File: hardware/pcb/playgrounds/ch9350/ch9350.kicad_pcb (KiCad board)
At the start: 2 copper layers, 50.8 x 76.2 mm, 35 parts, among them J1 TYPE-C-31-M-12, J2 USB-U267-BWS, J3 Conn_02x08_Odd_Even, J4 Conn_02x10_Odd_Even, J5 Conn_02x10_Odd_Even, Q1 MMBT2222A, Q2 MMBT2222A, Q3 MMBT2222A, Q4 MMBT2222A, Q5 MMBT2222A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

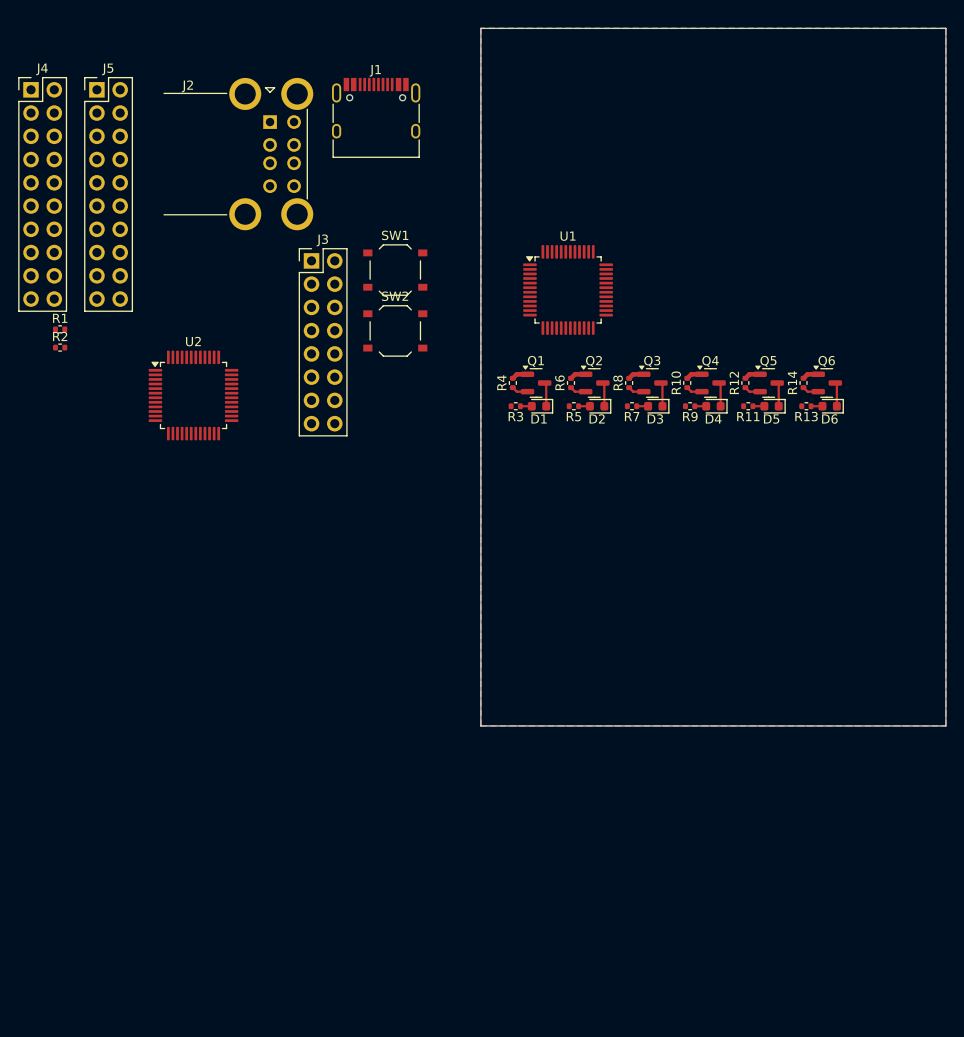
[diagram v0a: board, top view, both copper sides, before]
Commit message: ch9350 devboard layout
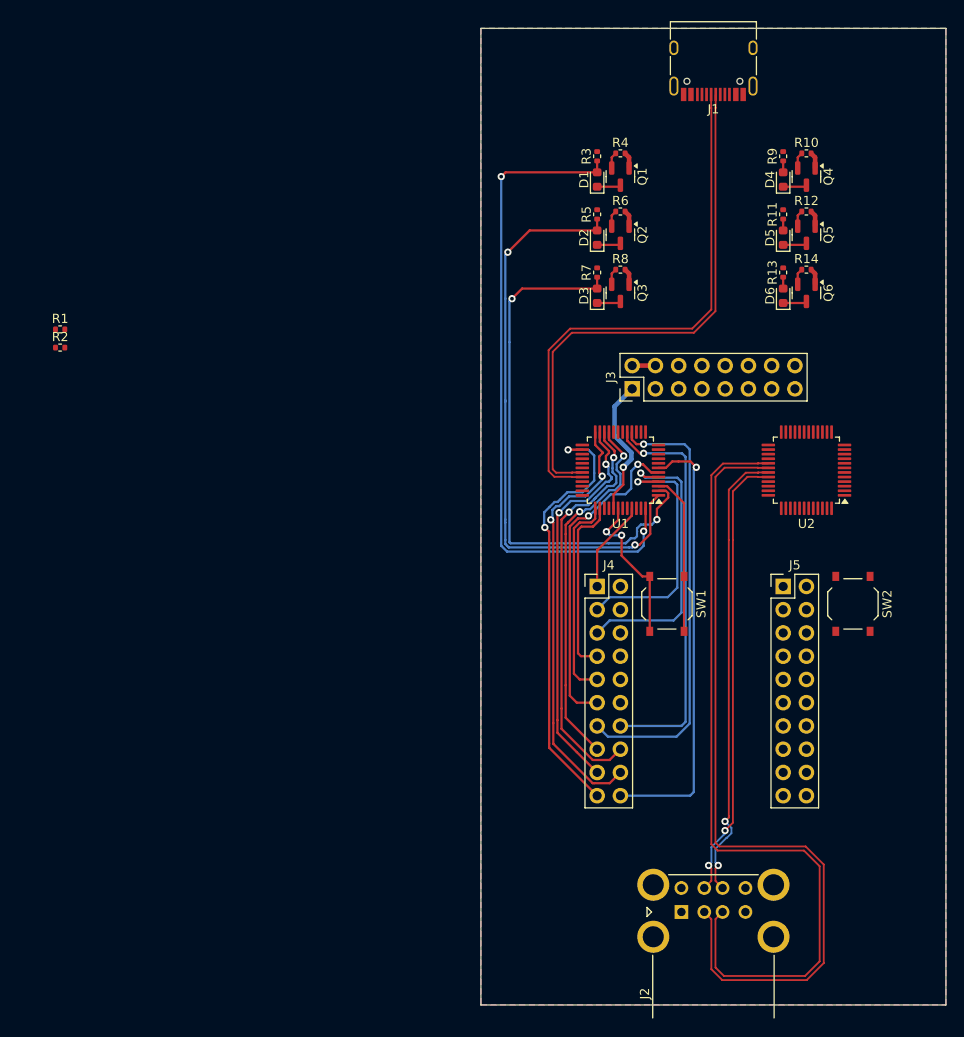
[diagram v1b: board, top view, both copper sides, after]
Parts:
- moved J2 97.3 mm to (148.9, 147.3), turned to 90 degrees
- moved J5 92.5 mm to (160.0, 111.8)
- moved J4 82.3 mm to (139.7, 111.8)
- moved U2 67.4 mm to (162.6, 99.1), turned to 180 degrees
- moved SW2 58.2 mm to (167.6, 113.7), turned to -90 degrees
- moved SW1 47.0 mm to (147.3, 113.7), turned to -90 degrees
- moved J3 37.7 mm to (143.5, 90.2), turned to 90 degrees
- moved J1 37.5 mm to (152.4, 54.0), turned to 180 degrees
- moved R9 29.1 mm to (160.0, 64.8), turned to 90 degrees
- moved R3 28.7 mm to (139.7, 64.8), turned to 90 degrees
- moved R10 28.3 mm to (162.6, 64.5), turned to 0 degrees
- moved R4 27.7 mm to (142.2, 64.5), turned to 0 degrees
- moved D4 25.9 mm to (160.0, 67.3), turned to 90 degrees
- moved D1 25.6 mm to (139.7, 67.3), turned to 90 degrees
- moved Q4 24.9 mm to (162.6, 67.0), turned to -90 degrees
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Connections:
- net /DM renamed /D-
- net /DM1 renamed /D1-
- net /DM2 renamed /D2-
- net /DP renamed /D+
- net /DP1 renamed /D1+
- net /DP2 renamed /D2+
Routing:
- net /D1-: track 0.00 -> 89.8 mm
- net /D1+: track 0.00 -> 89.1 mm
- net /LED0a: track 1.24 -> 72.5 mm, vias 0 -> 2
- net /LED1a: track 1.24 -> 65.2 mm, vias 0 -> 2
- net /D-: track 0.00 -> 60.3 mm
- net /D+: track 0.00 -> 59.5 mm
- net /LED2a: track 1.24 -> 60.0 mm, vias 0 -> 2
- net /D2+: track 0.00 -> 50.4 mm, vias 0 -> 2
- net /D2-: track 0.00 -> 49.4 mm, vias 0 -> 2
- net /XIa: track 0.00 -> 48.7 mm, vias 0 -> 1
- net /DEBUGa: track 0.00 -> 48.5 mm, vias 0 -> 1
- net /IO4a: track 0.00 -> 48.0 mm, vias 0 -> 2
- net /TNOWa: track 0.00 -> 47.7 mm, vias 0 -> 2
- net /IO2a: track 0.00 -> 45.3 mm, vias 0 -> 2
- net /XOa: track 0.00 -> 44.3 mm, vias 0 -> 1
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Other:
- board size 50.8 x 76.2 mm -> 50.8 x 106.7 mm

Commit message: ch9350 devboard layout
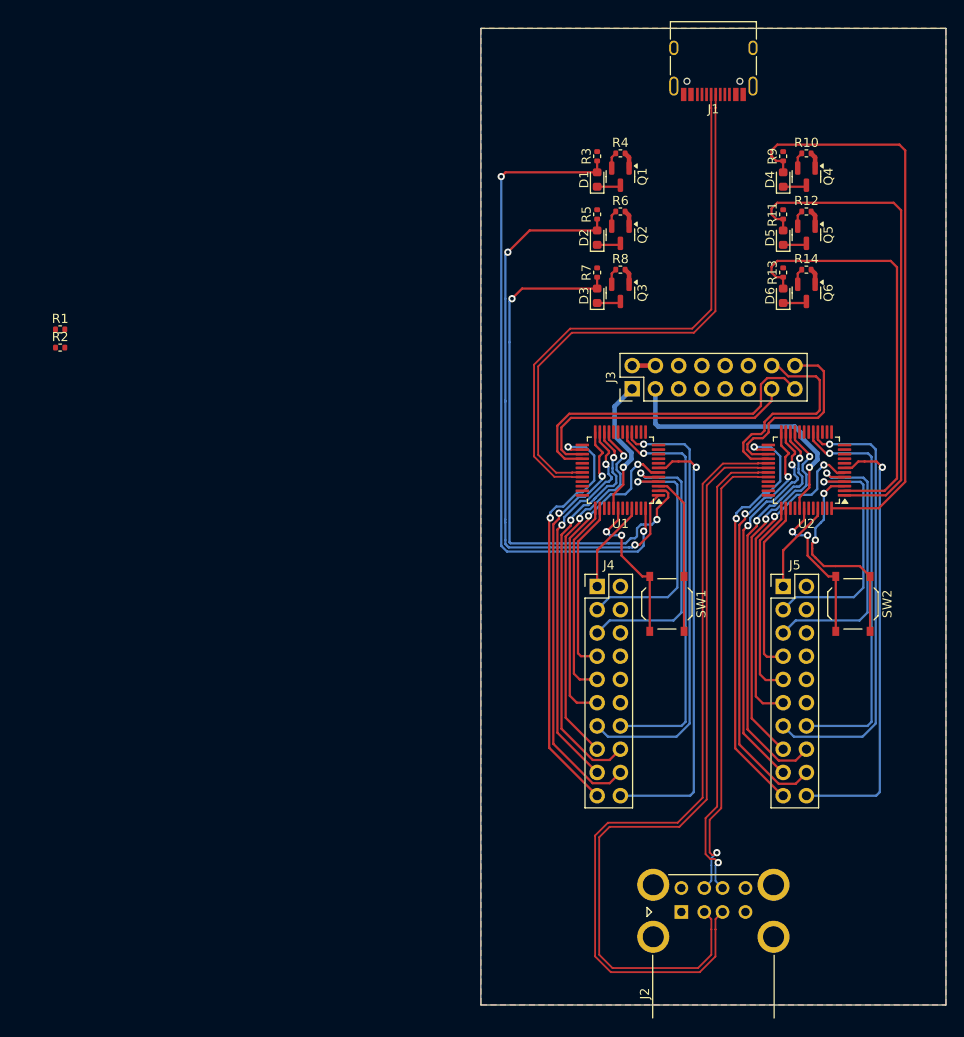
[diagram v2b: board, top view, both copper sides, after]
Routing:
- net /LED0b: track 1.24 -> 63.9 mm
- net /LED1b: track 1.24 -> 54.5 mm
- net /XIb: track 0.00 -> 48.7 mm, vias 0 -> 1
- net /DEBUGb: track 0.00 -> 48.5 mm, vias 0 -> 1
- net /IO4b: track 0.00 -> 47.1 mm, vias 0 -> 2
- net /TNOWb: track 0.00 -> 47.1 mm, vias 0 -> 2
- net /LED2b: track 1.24 -> 47.0 mm
- net /IO2b: track 0.00 -> 44.8 mm, vias 0 -> 2
- net /XOb: track 0.00 -> 44.3 mm, vias 0 -> 1
- net /IO3b: track 0.00 -> 42.8 mm, vias 0 -> 2
- net /IO1b: track 0.00 -> 40.3 mm, vias 0 -> 2
- net /TXDa: track 0.00 -> 35.8 mm
- net /xOSCb: track 0.00 -> 35.3 mm, vias 0 -> 2
- net /S1b: track 0.00 -> 31.4 mm, vias 0 -> 1
- net /RXDa: track 0.00 -> 30.4 mm
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
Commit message: ch9350 devboard layout
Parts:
- moved R1 77.3 mm to (154.7, 60.3)
- moved R2 73.3 mm to (149.9, 60.3), turned to 180 degrees
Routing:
- net /VBUS: track 2.54 -> 184.8 mm, vias 0 -> 2
- net GNDPWR: track 0.00 -> 25.5 mm
- net GND: track 10.7 -> 15.6 mm
- net /CC1: track 0.00 -> 2.55 mm
- net /CC2: track 0.00 -> 2.42 mm
- net /TXDb: track 23.6 -> 23.0 mm

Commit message: ch9350 devboard layout 2
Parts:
- removed D1, D2, D3, D4, D5, D6: 19-213/Y2C-CQ2R2L/3T(CY), LED_SMD:LED_0603_1608Metric
- removed J1: TYPE-C-31-M-12, Connector_USB:USB_C_Receptacle_HRO_TYPE-C-31-M-12
- removed J2: USB-U267-BWS, Connector_USB:USB_A_CUI_UJ2-ADH-TH_Horizontal_Stacked
- removed J3: Conn_02x08_Odd_Even, Connector_PinHeader_2.54mm:PinHeader_2x08_P2.54mm_Vertical
- removed J4, J5: Conn_02x10_Odd_Even, Connector_PinHeader_2.54mm:PinHeader_2x10_P2.54mm_Vertical
- removed Q1, Q2, Q3, Q4, Q5, Q6: MMBT2222A, Package_TO_SOT_SMD:SOT-23
- removed R1, R2: 5K1, Resistor_SMD:R_0402_1005Metric
- removed R10, R12, R14, R4, R6, R8: 6K2, Resistor_SMD:R_0402_1005Metric
- removed R11, R13, R3, R5, R7, R9: 1K, Resistor_SMD:R_0402_1005Metric
- removed SW1, SW2: TS-1187A-B-A-B, Button_Switch_SMD:SW_Push_1P1T_XKB_TS-1187A
- removed U1, U2: CH9350, Package_QFP:LQFP-48_7x7mm_P0.5mm
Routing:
- net /VBUS: track 184.8 -> 0.00 mm, vias 2 -> 0
- net /D1+: track 88.8 -> 0.00 mm
- net /D1-: track 86.6 -> 0.00 mm
- net /LED0a: track 72.5 -> 0.00 mm, vias 2 -> 0
- net /LED1a: track 65.2 -> 0.00 mm, vias 2 -> 0
- net /LED0b: track 63.9 -> 0.00 mm
- net /D-: track 61.6 -> 0.00 mm
- net /D+: track 60.8 -> 0.00 mm
- net /LED2a: track 60.0 -> 0.00 mm, vias 2 -> 0
- net /LED1b: track 54.5 -> 0.00 mm
- net /D2+: track 51.9 -> 0.00 mm, vias 1 -> 0
- net /D2-: track 51.4 -> 0.00 mm, vias 1 -> 0
- net /XIa: track 48.7 -> 0.00 mm, vias 1 -> 0
- net /XIb: track 48.7 -> 0.00 mm, vias 1 -> 0
- net /DEBUGb: track 48.5 -> 0.00 mm, vias 1 -> 0
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
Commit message: ch9350 devboard layout 2
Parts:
- added D1: 19-213/Y2C-CQ2R2L/3T(CY), LED_SMD:LED_0603_1608Metric, F.Cu at (78.8, 79.5)
- added D2: 19-213/Y2C-CQ2R2L/3T(CY), LED_SMD:LED_0603_1608Metric, F.Cu at (78.8, 82.1)
- added D3: 19-213/Y2C-CQ2R2L/3T(CY), LED_SMD:LED_0603_1608Metric, F.Cu at (78.8, 84.7)
- added D4: 19-213/Y2C-CQ2R2L/3T(CY), LED_SMD:LED_0603_1608Metric, F.Cu at (78.8, 87.3)
- added D5: 19-213/Y2C-CQ2R2L/3T(CY), LED_SMD:LED_0603_1608Metric, F.Cu at (78.8, 89.9)
- added D6: 19-213/Y2C-CQ2R2L/3T(CY), LED_SMD:LED_0603_1608Metric, F.Cu at (78.8, 92.5)
- added J1: TYPE-C-31-M-12, Connector_USB:USB_C_Receptacle_HRO_TYPE-C-31-M-12, F.Cu at (152.4, 54.6)
- added J2: USB-U267-BWS, Connector_USB:USB_A_CUI_UJ2-ADH-TH_Horizontal_Stacked, F.Cu at (105.2, 56.6)
- added J3: Conn_02x08_Odd_Even, Connector_PinHeader_2.54mm:PinHeader_2x08_P2.54mm_Vertical, F.Cu at (143.5, 99.1)
- added J4: Conn_02x10_Odd_Even, Connector_PinHeader_2.54mm:PinHeader_2x10_P2.54mm_Vertical, F.Cu at (170.2, 67.3)
- added J5: Conn_02x10_Odd_Even, Connector_PinHeader_2.54mm:PinHeader_2x10_P2.54mm_Vertical, F.Cu at (86.3, 53.1)
- added Q1: MMBT2222A, Package_TO_SOT_SMD:SOT-23, F.Cu at (105.0, 71.8)
- added Q2: MMBT2222A, Package_TO_SOT_SMD:SOT-23, F.Cu at (105.0, 76.5)
- added Q3: MMBT2222A, Package_TO_SOT_SMD:SOT-23, F.Cu at (105.0, 81.1)
- added Q4: MMBT2222A, Package_TO_SOT_SMD:SOT-23, F.Cu at (105.0, 85.7)
- added Q5: MMBT2222A, Package_TO_SOT_SMD:SOT-23, F.Cu at (105.0, 90.3)
- added Q6: MMBT2222A, Package_TO_SOT_SMD:SOT-23, F.Cu at (105.0, 95.0)
- added R1: 5K1, Resistor_SMD:R_0402_1005Metric, F.Cu at (82.3, 79.2)
- added R10: 6K2, Resistor_SMD:R_0402_1005Metric, F.Cu at (85.2, 87.2)
- added R11: 1K, Resistor_SMD:R_0402_1005Metric, F.Cu at (88.1, 79.2)
- added R12: 6K2, Resistor_SMD:R_0402_1005Metric, F.Cu at (88.1, 81.2)
- added R13: 1K, Resistor_SMD:R_0402_1005Metric, F.Cu at (88.1, 83.2)
- added R14: 6K2, Resistor_SMD:R_0402_1005Metric, F.Cu at (88.1, 85.2)
- added R2: 5K1, Resistor_SMD:R_0402_1005Metric, F.Cu at (82.3, 81.2)
- added R3: 1K, Resistor_SMD:R_0402_1005Metric, F.Cu at (82.3, 83.2)
- added R4: 6K2, Resistor_SMD:R_0402_1005Metric, F.Cu at (82.3, 85.2)
- added R5: 1K, Resistor_SMD:R_0402_1005Metric, F.Cu at (82.3, 87.2)
- added R6: 6K2, Resistor_SMD:R_0402_1005Metric, F.Cu at (85.2, 79.2)
- added R7: 1K, Resistor_SMD:R_0402_1005Metric, F.Cu at (85.2, 81.2)
- added R8: 6K2, Resistor_SMD:R_0402_1005Metric, F.Cu at (85.2, 83.2)
- added R9: 1K, Resistor_SMD:R_0402_1005Metric, F.Cu at (85.2, 85.2)
- added SW1: TS-1187A-B-A-B, Button_Switch_SMD:SW_Push_1P1T_XKB_TS-1187A, F.Cu at (118.9, 72.8)
- added SW2: TS-1187A-B-A-B, Button_Switch_SMD:SW_Push_1P1T_XKB_TS-1187A, F.Cu at (118.9, 79.4)
- added U1: CH9350, Package_QFP:LQFP-48_7x7mm_P0.5mm, F.Cu at (152.4, 78.7)
- added U2: CH9350, Package_QFP:LQFP-48_7x7mm_P0.5mm, F.Cu at (96.9, 86.5)
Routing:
- net /VBUS: track 0.00 -> 53.8 mm, vias 0 -> 2
- net /VBUSa: track 0.00 -> 32.3 mm, vias 0 -> 3
- net /SELa: track 0.00 -> 31.5 mm, vias 0 -> 1
- net /DEBUGa: track 0.00 -> 31.2 mm, vias 0 -> 2
- net /RXDa: track 0.00 -> 29.6 mm, vias 0 -> 1
- net /TXDa: track 0.00 -> 28.0 mm, vias 0 -> 1
- net /S0a: track 0.00 -> 27.1 mm, vias 0 -> 2
- net /S1a: track 0.00 -> 25.9 mm, vias 0 -> 2
- net /TNOWa: track 0.00 -> 24.6 mm, vias 0 -> 1
- net /xOSCa: track 0.00 -> 24.4 mm, vias 0 -> 2
- net /BAUD0a: track 0.00 -> 23.4 mm, vias 0 -> 1
- net /BAUD1a: track 0.00 -> 23.2 mm, vias 0 -> 1
- net /XOa: track 0.00 -> 21.3 mm, vias 0 -> 2
- net /XIa: track 0.00 -> 18.6 mm, vias 0 -> 2
- net /D+: track 0.00 -> 18.6 mm
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
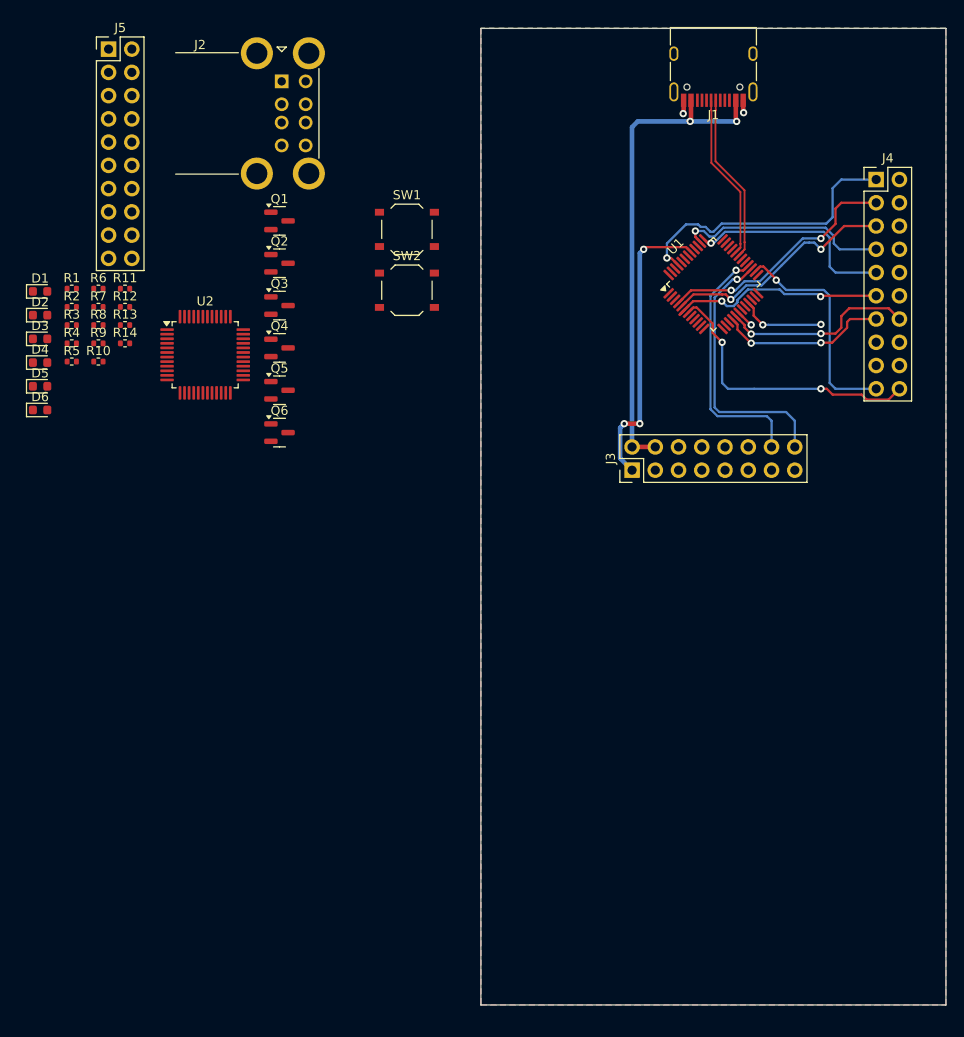
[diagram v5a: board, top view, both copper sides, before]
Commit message: ch9350 devboard layout 3
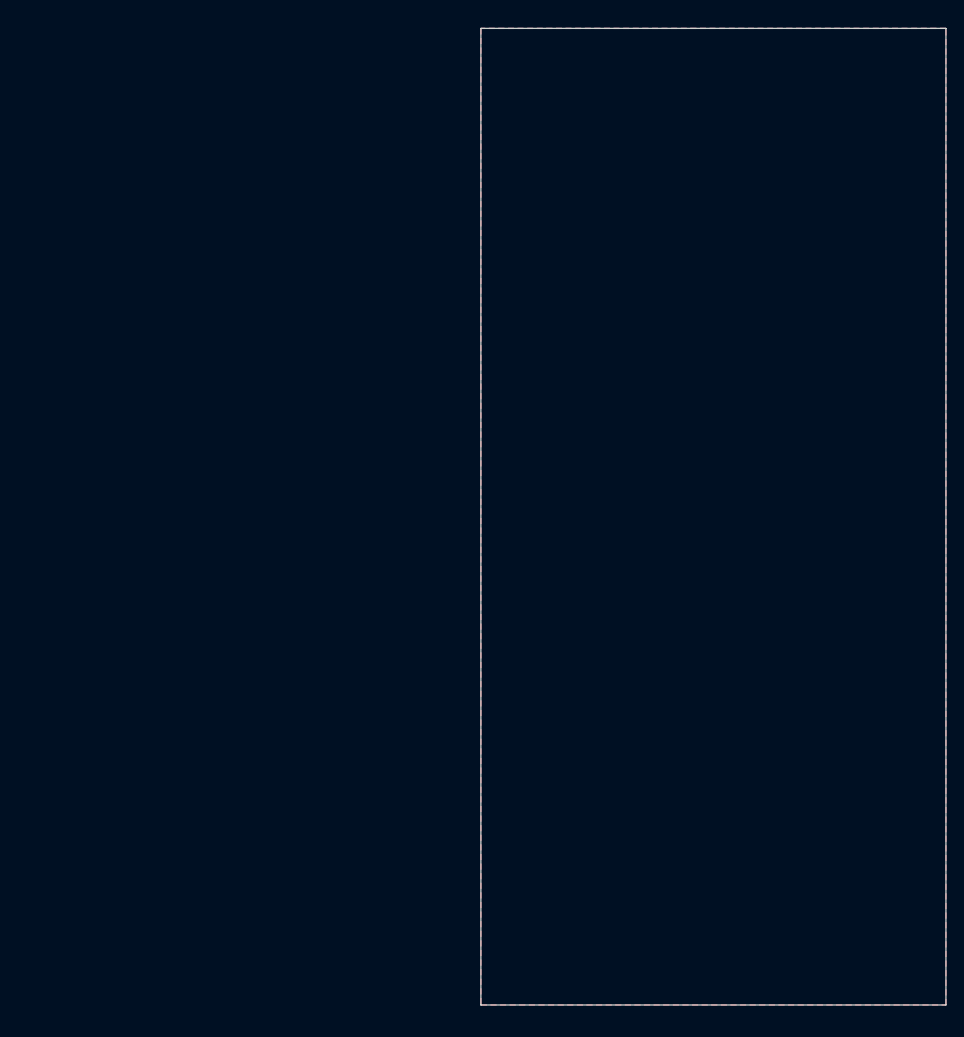
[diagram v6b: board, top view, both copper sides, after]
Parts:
- removed D1, D2, D3, D4, D5, D6: 19-213/Y2C-CQ2R2L/3T(CY), LED_SMD:LED_0603_1608Metric
- removed J1: TYPE-C-31-M-12, Connector_USB:USB_C_Receptacle_HRO_TYPE-C-31-M-12
- removed J2: USB-U267-BWS, Connector_USB:USB_A_CUI_UJ2-ADH-TH_Horizontal_Stacked
- removed J3: Conn_02x08_Odd_Even, Connector_PinHeader_2.54mm:PinHeader_2x08_P2.54mm_Vertical
- removed J4, J5: Conn_02x10_Odd_Even, Connector_PinHeader_2.54mm:PinHeader_2x10_P2.54mm_Vertical
- removed Q1, Q2, Q3, Q4, Q5, Q6: MMBT2222A, Package_TO_SOT_SMD:SOT-23
- removed R1, R2: 5K1, Resistor_SMD:R_0402_1005Metric
- removed R10, R12, R14, R4, R6, R8: 6K2, Resistor_SMD:R_0402_1005Metric
- removed R11, R13, R3, R5, R7, R9: 1K, Resistor_SMD:R_0402_1005Metric
- removed SW1, SW2: TS-1187A-B-A-B, Button_Switch_SMD:SW_Push_1P1T_XKB_TS-1187A
- removed U1, U2: CH9350, Package_QFP:LQFP-48_7x7mm_P0.5mm
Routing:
- net /VBUS: track 53.8 -> 0.00 mm, vias 2 -> 0
- net /VBUSa: track 32.3 -> 0.00 mm, vias 3 -> 0
- net /SELa: track 31.5 -> 0.00 mm, vias 1 -> 0
- net /DEBUGa: track 31.2 -> 0.00 mm, vias 2 -> 0
- net /RXDa: track 29.6 -> 0.00 mm, vias 1 -> 0
- net /TXDa: track 28.0 -> 0.00 mm, vias 1 -> 0
- net /S0a: track 27.1 -> 0.00 mm, vias 2 -> 0
- net /S1a: track 25.9 -> 0.00 mm, vias 2 -> 0
- net /TNOWa: track 24.6 -> 0.00 mm, vias 1 -> 0
- net /xOSCa: track 24.4 -> 0.00 mm, vias 2 -> 0
- net /BAUD0a: track 23.4 -> 0.00 mm, vias 1 -> 0
- net /BAUD1a: track 23.2 -> 0.00 mm, vias 1 -> 0
- net /XOa: track 21.3 -> 0.00 mm, vias 2 -> 0
- net /XIa: track 18.6 -> 0.00 mm, vias 2 -> 0
- net /D+: track 18.6 -> 0.00 mm
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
